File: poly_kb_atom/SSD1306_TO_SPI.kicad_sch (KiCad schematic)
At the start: 12 parts

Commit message: Final version of wave
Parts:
- C1_1, C2_1: value 2.2uF -> (none); footprint Capacitor_SMD:C_0603_1608Metric -> (none)
- C3_1, C5_1, C6_1: value 1uF -> (none); footprint Capacitor_SMD:C_0402_1005Metric -> (none)
- C4_1: value 4.7uF -> (none); footprint Capacitor_SMD:C_0603_1608Metric -> (none)
- C7_1: value DNP -> (none); footprint Capacitor_SMD:C_0603_1608Metric -> (none)
- CONN1: value 0.42" Display Connector -> (none); footprint poly_kb:FPC_16_JUSHUO_AFC05_S16FIA_00 -> (none)
- D1_1: value D_Small -> (none); footprint poly_kb:D_SOD-323Ext -> (none)
- LED1: value WS2812B-Mini -> (none); footprint poly_kb:WS2812B-Mini -> (none)
- R1_1: value 10k -> (none); footprint Resistor_SMD:R_0402_1005Metric -> (none); LCSC (none) -> C25744
- SW_K_1: value CheeryMX KeySwitch -> (none); footprint poly_kb:SW_Cherry_MX_1.00u_PCB_NoSilk -> (none)
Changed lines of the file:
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@@
       (effects (font (size 1.27 1.27)) (justify left))
     )
-    (property "Value" "0.42\" Display Connector" (id 1) (at 76.2 30.48 0)
-      (effects (font (size 1.27 1.27)) (justify left))
-    )
-    (property "Footprint" "poly_kb:FPC_16_JUSHUO_AFC05_S16FIA_00" (id 2) (at 82.55 52.07 0)
+    (property "Value" "" (id 1) (at 76.2 30.48 0)
+      (effects (font (size 1.27 1.27)) (justify left))
+    )
+    (property "Footprint" "" (id 2) (at 82.55 52.07 0)
       (effects (font (size 1.27 1.27)) hide)
     )
@@
     (in_bom yes) (on_board yes)
     (property "Reference" "C6_1" (id 0) (at 63.5 45.72 90))
-    (property "Value" "1uF" (id 1) (at 63.5 48.26 90))
-    (property "Footprint" "Capacitor_SMD:C_0402_1005Metric" (id 2) (at 68.58 46.99 0)
+    (property "Value" "" (id 1) (at 63.5 48.26 90))
+    (property "Footprint" "" (id 2) (at 68.58 46.99 0)
       (effects (font (size 1.27 1.27)) hide)
     )
@@
       (effects (font (size 1.27 1.27)) (justify left))
     )
-    (property "Value" "WS2812B-Mini" (id 1) (at 175.26 54.61 0)
-      (effects (font (size 1.27 1.27)) (justify left))
-    )
-    (property "Footprint" "poly_kb:WS2812B-Mini" (id 2) (at 167.64 55.88 0)
+    (property "Value" "" (id 1) (at 175.26 54.61 0)
+      (effects (font (size 1.27 1.27)) (justify left))
+    )
+    (property "Footprint" "" (id 2) (at 167.64 55.88 0)
       (effects (font (size 1.27 1.27)) (justify left top) hide)
     )
@@
       (effects (font (size 1.27 1.27)) (justify right))
     )
-    (property "Value" "4.7uF" (id 1) (at 57.15 76.2 90)
-      (effects (font (size 1.27 1.27)) (justify right))
-    )
-    (property "Footprint" "Capacitor_SMD:C_0603_1608Metric" (id 2) (at 54.61 69.85 0)
+    (property "Value" "" (id 1) (at 57.15 76.2 90)
+      (effects (font (size 1.27 1.27)) (justify right))
+    )
+    (property "Footprint" "" (id 2) (at 54.61 69.85 0)
       (effects (font (size 1.27 1.27)) hide)
     )
@@
     (in_bom yes) (on_board yes)
     (property "Reference" "C1_1" (id 0) (at 71.12 74.93 0))
-    (property "Value" "2.2uF" (id 1) (at 71.12 77.47 0))
-    (property "Footprint" "Capacitor_SMD:C_0603_1608Metric" (id 2) (at 67.31 74.93 0)
+    (property "Value" "" (id 1) (at 71.12 77.47 0))
+    (property "Footprint" "" (id 2) (at 67.31 74.93 0)
       (effects (font (size 1.27 1.27)) hide)
     )
@@
     (in_bom yes) (on_board yes)
     (property "Reference" "C5_1" (id 0) (at 57.15 36.0934 90))
-    (property "Value" "1uF" (id 1) (at 57.15 38.4048 90))
-    (property "Footprint" "Capacitor_SMD:C_0402_1005Metric" (id 2) (at 57.15 41.91 0)
+    (property "Value" "" (id 1) (at 57.15 38.4048 90))
+    (property "Footprint" "" (id 2) (at 57.15 41.91 0)
       (effects (font (size 1.27 1.27)) hide)
     )
@@
     (in_bom yes) (on_board yes)
     (property "Reference" "C2_1" (id 0) (at 46.99 46.2534 90))
-    (property "Value" "2.2uF" (id 1) (at 46.99 48.5648 90))
-    (property "Footprint" "Capacitor_SMD:C_0603_1608Metric" (id 2) (at 46.99 52.07 0)
+    (property "Value" "" (id 1) (at 46.99 48.5648 90))
+    (property "Footprint" "" (id 2) (at 46.99 52.07 0)
       (effects (font (size 1.27 1.27)) hide)
     )
@@
     (in_bom yes) (on_board yes)
     (property "Reference" "C3_1" (id 0) (at 31.75 42.4434 90))
-    (property "Value" "1uF" (id 1) (at 31.75 44.7548 90))
-    (property "Footprint" "Capacitor_SMD:C_0402_1005Metric" (id 2) (at 31.75 48.26 0)
+    (property "Value" "" (id 1) (at 31.75 44.7548 90))
+    (property "Footprint" "" (id 2) (at 31.75 48.26 0)
       (effects (font (size 1.27 1.27)) hide)
     )
@@
     (in_bom yes) (on_board yes)
     (property "Reference" "SW_K_1" (id 0) (at 129.54 82.931 0))
-    (property "Value" "CheeryMX KeySwitch" (id 1) (at 129.54 85.2424 0))
-    (property "Footprint" "poly_kb:SW_Cherry_MX_1.00u_PCB_NoSilk" (id 2) (at 129.54 85.09 0)
+    (property "Value" "" (id 1) (at 129.54 85.2424 0))
+    (property "Footprint" "" (id 2) (at 129.54 85.09 0)
       (effects (font (size 1.27 1.27)) hide)
     )
@@
     (in_bom yes) (on_board yes)
     (property "Reference" "D1_1" (id 0) (at 139.7 95.4278 0))
-    (property "Value" "D_Small" (id 1) (at 139.7 93.1164 0))
-    (property "Footprint" "poly_kb:D_SOD-323Ext" (id 2) (at 139.7 90.17 90)
+    (property "Value" "" (id 1) (at 139.7 93.1164 0))
+    (property "Footprint" "" (id 2) (at 139.7 90.17 90)
       (effects (font (size 1.27 1.27)) hide)
     )
@@
       (effects (font (size 1.27 1.27)) (justify right))
     )
-    (property "Value" "DNP" (id 1) (at 142.24 45.72 0)
-      (effects (font (size 1.27 1.27)) (justify right))
-    )
-    (property "Footprint" "Capacitor_SMD:C_0603_1608Metric" (id 2) (at 142.24 48.26 0)
+    (property "Value" "" (id 1) (at 142.24 45.72 0)
+      (effects (font (size 1.27 1.27)) (justify right))
+    )
+    (property "Footprint" "" (id 2) (at 142.24 48.26 0)
       (effects (font (size 1.27 1.27)) hide)
     )
@@
       (effects (font (size 1.27 1.27)) (justify left))
     )
-    (property "Value" "10k" (id 1) (at 34.5186 58.293 0)
-      (effects (font (size 1.27 1.27)) (justify left))
-    )
-    (property "Footprint" "Resistor_SMD:R_0402_1005Metric" (id 2) (at 33.02 57.15 0)
+    (property "Value" "" (id 1) (at 34.5186 58.293 0)
+      (effects (font (size 1.27 1.27)) (justify left))
+    )
+    (property "Footprint" "" (id 2) (at 33.02 57.15 0)
       (effects (font (size 1.27 1.27)) hide)
     )
@@
       (effects (font (size 1.27 1.27)) hide)
     )
+    (property "LCSC" "C25744" (id 4) (at 33.02 57.15 0)
+      (effects (font (size 1.27 1.27)) hide)
+    )

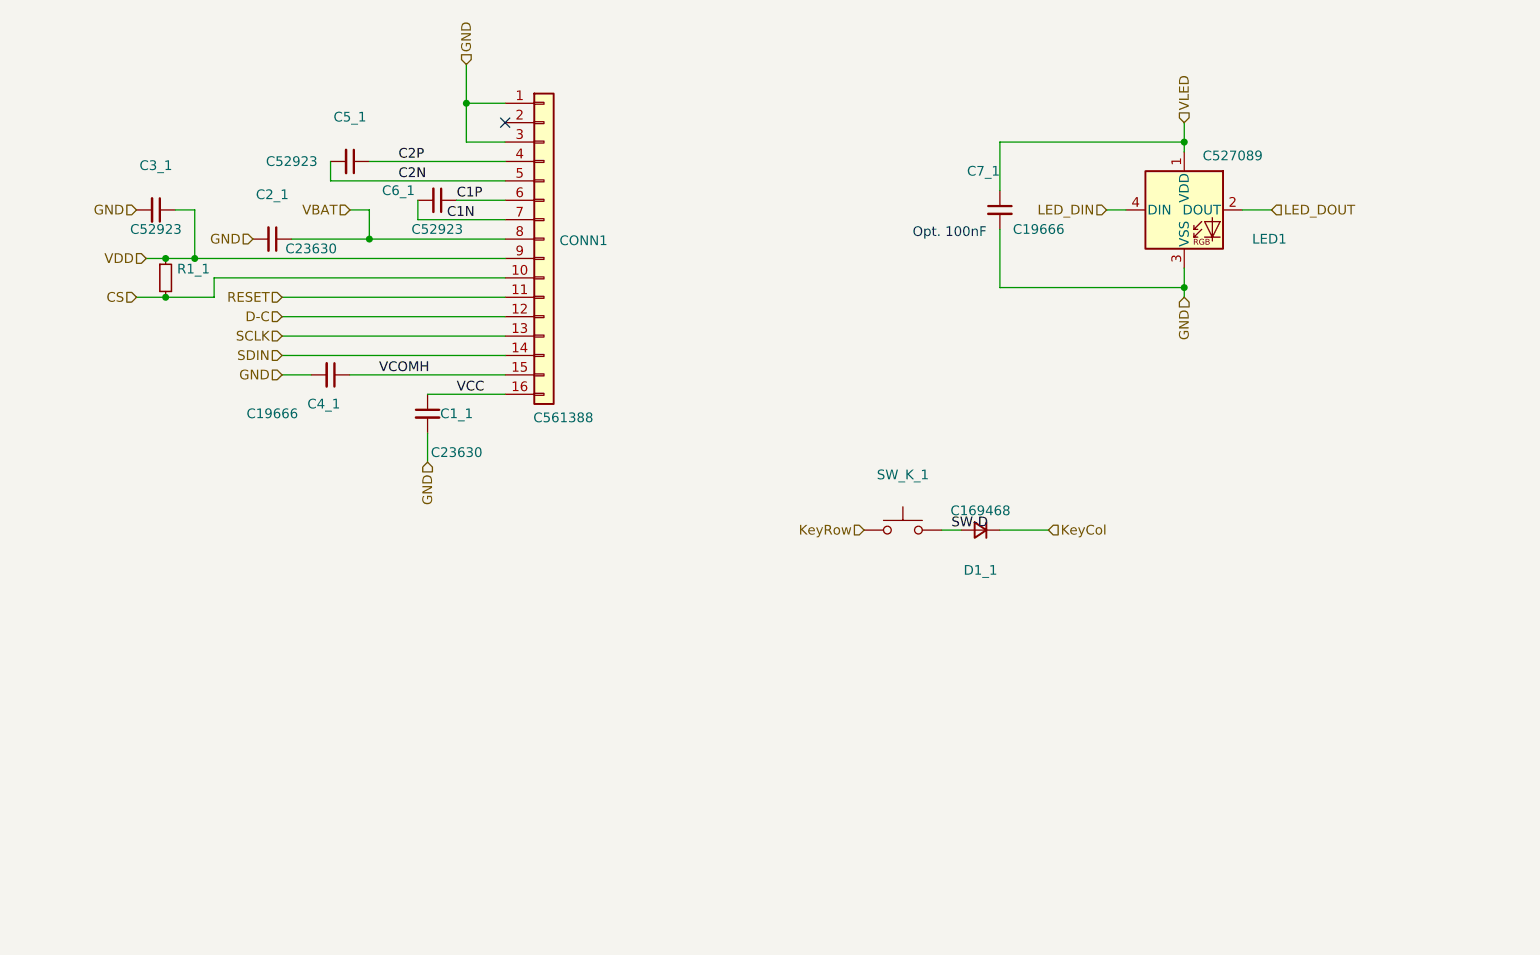
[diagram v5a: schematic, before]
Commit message: Added power leds
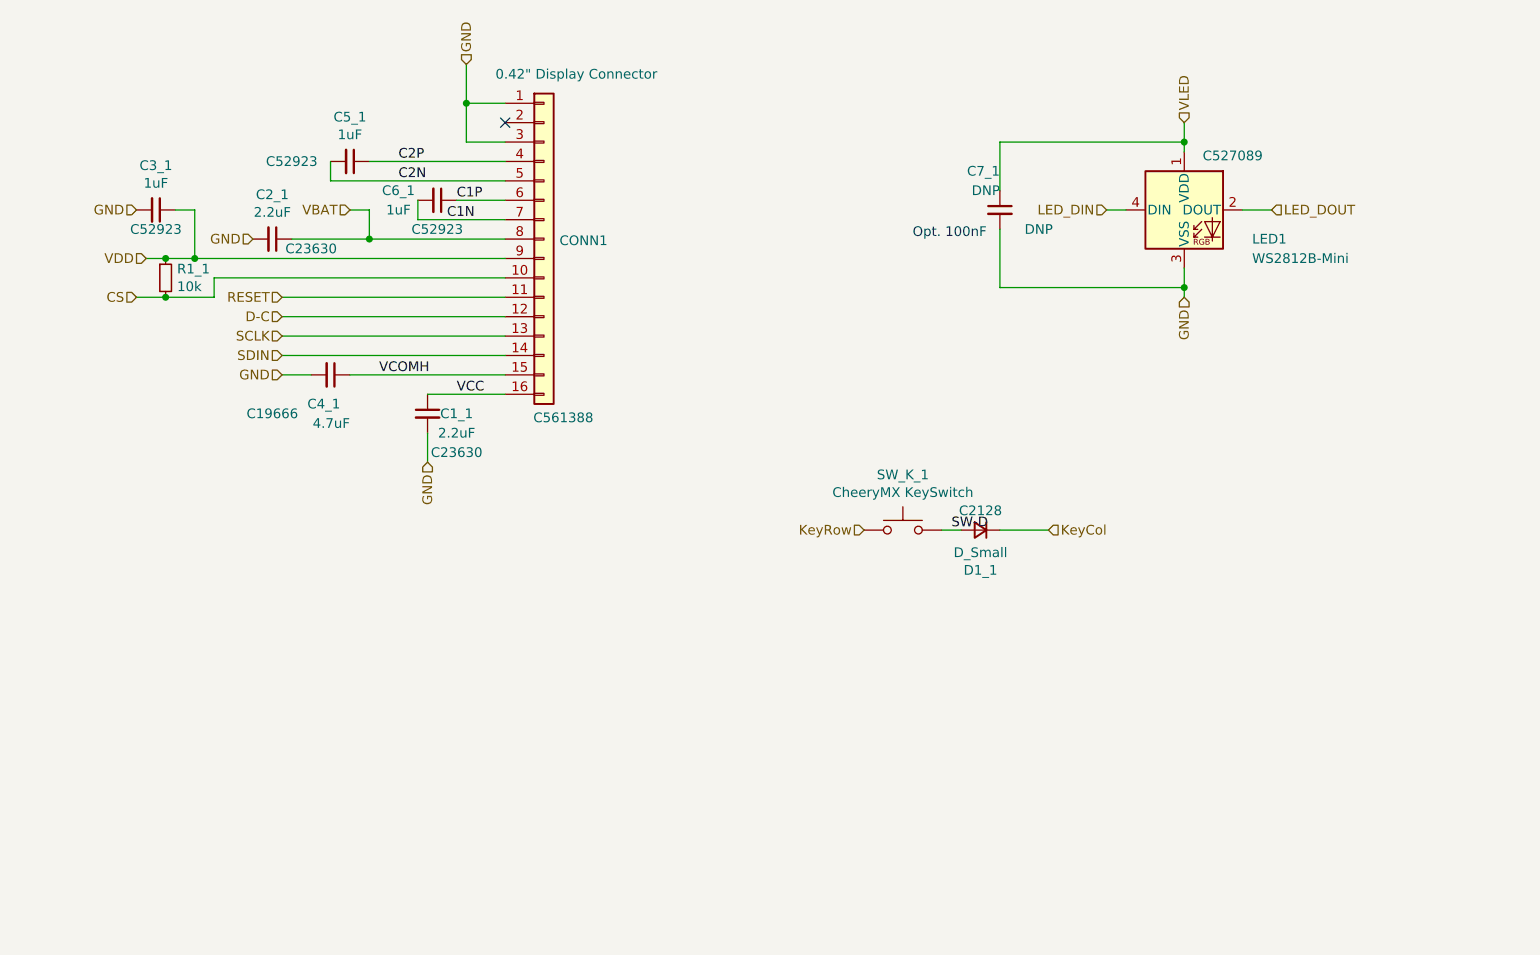
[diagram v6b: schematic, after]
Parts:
- C1_1, C2_1: value (none) -> 2.2uF; JLC (none) -> 0603; LCSC C23630 -> C23630
- C3_1, C5_1, C6_1: value (none) -> 1uF; JLC (none) -> 0402; LCSC C52923 -> C52923
- C4_1: value (none) -> 4.7uF; JLC (none) -> 0603
- C7_1: value (none) -> DNP; JLC (none) -> DNP; LCSC C19666 -> DNP
- CONN1: value (none) -> 0.42" Display Connector; JLC (none) -> AtomConnect2
- D1_1: value (none) -> D_Small; JLC (none) -> D_SOD-323Ext; LCSC C169468 -> C2128
- LED1: value (none) -> WS2812B-Mini; JLC (none) -> WS2812B-Mini
- R1_1: value (none) -> 10k; JLC (none) -> 0402
- SW_K_1: value (none) -> CheeryMX KeySwitch
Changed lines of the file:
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@@
       (effects (font (size 1.27 1.27)) (justify left))
     )
-    (property "Value" "" (id 1) (at 76.2 30.48 0)
+    (property "Value" "0.42\" Display Connector" (id 1) (at 76.2 30.48 0)
       (effects (font (size 1.27 1.27)) (justify left))
     )
@@
     (property "LCSC" "C561388" (id 4) (at 85.09 76.2 0)
       (effects (font (size 1.27 1.27)) (justify bottom))
+    )
+    (property "JLC" "AtomConnect2" (id 5) (at 82.55 52.07 0)
+      (effects (font (size 1.27 1.27)) hide)
     )
     (pin "1")
@@
     (in_bom yes) (on_board yes)
     (property "Reference" "C6_1" (id 0) (at 63.5 45.72 90))
-    (property "Value" "" (id 1) (at 63.5 48.26 90))
+    (property "Value" "1uF" (id 1) (at 63.5 48.26 90))
     (property "Footprint" "" (id 2) (at 68.58 46.99 0)
       (effects (font (size 1.27 1.27)) hide)
@@
       (effects (font (size 1.27 1.27)) hide)
     )
-    (property "LCSC" " C52923" (id 4) (at 68.58 50.8 90))
+    (property "LCSC" "C52923" (id 4) (at 68.58 50.8 90))
+    (property "JLC" "0402" (id 5) (at 68.58 46.99 0)
+      (effects (font (size 1.27 1.27)) hide)
+    )
     (pin "1")
     (pin "2")
@@
       (effects (font (size 1.27 1.27)) (justify left))
     )
-    (property "Value" "" (id 1) (at 175.26 54.61 0)
+    (property "Value" "WS2812B-Mini" (id 1) (at 175.26 54.61 0)
       (effects (font (size 1.27 1.27)) (justify left))
     )
@@
       (effects (font (size 1.27 1.27)) (justify bottom))
     )
+    (property "JLC" "WS2812B-Mini" (id 5) (at 166.37 48.26 0)
+      (effects (font (size 1.27 1.27)) hide)
+    )
     (pin "1")
     (pin "2")
@@
       (effects (font (size 1.27 1.27)) (justify right))
     )
-    (property "Value" "" (id 1) (at 57.15 76.2 90)
+    (property "Value" "4.7uF" (id 1) (at 57.15 76.2 90)
       (effects (font (size 1.27 1.27)) (justify right))
     )
@@
     )
     (property "LCSC" "C19666" (id 4) (at 46.99 74.93 90))
+    (property "JLC" "0603" (id 5) (at 54.61 69.85 0)
+      (effects (font (size 1.27 1.27)) hide)
+    )
     (pin "1")
     (pin "2")
@@
     (in_bom yes) (on_board yes)
     (property "Reference" "C1_1" (id 0) (at 71.12 74.93 0))
-    (property "Value" "" (id 1) (at 71.12 77.47 0))
+    (property "Value" "2.2uF" (id 1) (at 71.12 77.47 0))
     (property "Footprint" "" (id 2) (at 67.31 74.93 0)
       (effects (font (size 1.27 1.27)) hide)
@@
       (effects (font (size 1.27 1.27)) hide)
     )
-    (property "LCSC" " C23630" (id 4) (at 71.12 80.01 0))
+    (property "LCSC" "C23630" (id 4) (at 71.12 80.01 0))
+    (property "JLC" "0603" (id 5) (at 67.31 74.93 0)
+      (effects (font (size 1.27 1.27)) hide)
+    )
     (pin "1")
     (pin "2")
@@
     (in_bom yes) (on_board yes)
     (property "Reference" "C5_1" (id 0) (at 57.15 36.0934 90))
-    (property "Value" "" (id 1) (at 57.15 38.4048 90))
+    (property "Value" "1uF" (id 1) (at 57.15 38.4048 90))
     (property "Footprint" "" (id 2) (at 57.15 41.91 0)
       (effects (font (size 1.27 1.27)) hide)
@@
       (effects (font (size 1.27 1.27)) hide)
     )
-    (property "LCSC" " C52923" (id 4) (at 49.53 41.91 90))
+    (property "LCSC" "C52923" (id 4) (at 49.53 41.91 90))
+    (property "JLC" "0402" (id 5) (at 57.15 41.91 0)
+      (effects (font (size 1.27 1.27)) hide)
+    )
     (pin "1")
     (pin "2")
@@
     (in_bom yes) (on_board yes)
     (property "Reference" "C2_1" (id 0) (at 46.99 46.2534 90))
-    (property "Value" "" (id 1) (at 46.99 48.5648 90))
+    (property "Value" "2.2uF" (id 1) (at 46.99 48.5648 90))
     (property "Footprint" "" (id 2) (at 46.99 52.07 0)
       (effects (font (size 1.27 1.27)) hide)
@@
       (effects (font (size 1.27 1.27)) hide)
     )
-    (property "LCSC" " C23630" (id 4) (at 52.07 53.34 90))
+    (property "LCSC" "C23630" (id 4) (at 52.07 53.34 90))
+    (property "JLC" "0603" (id 5) (at 46.99 52.07 0)
+      (effects (font (size 1.27 1.27)) hide)
+    )
     (pin "1")
     (pin "2")
@@
     (in_bom yes) (on_board yes)
     (property "Reference" "C3_1" (id 0) (at 31.75 42.4434 90))
-    (property "Value" "" (id 1) (at 31.75 44.7548 90))
+    (property "Value" "1uF" (id 1) (at 31.75 44.7548 90))
     (property "Footprint" "" (id 2) (at 31.75 48.26 0)
       (effects (font (size 1.27 1.27)) hide)
@@
       (effects (font (size 1.27 1.27)) hide)
     )
-    (property "LCSC" " C52923" (id 4) (at 31.75 50.8 90))
+    (property "LCSC" "C52923" (id 4) (at 31.75 50.8 90))
+    (property "JLC" "0402" (id 5) (at 31.75 48.26 0)
+      (effects (font (size 1.27 1.27)) hide)
+    )
     (pin "1")
     (pin "2")
@@
     (in_bom yes) (on_board yes)
     (property "Reference" "SW_K_1" (id 0) (at 129.54 82.931 0))
-    (property "Value" "" (id 1) (at 129.54 85.2424 0))
+    (property "Value" "CheeryMX KeySwitch" (id 1) (at 129.54 85.2424 0))
     (property "Footprint" "" (id 2) (at 129.54 85.09 0)
       (effects (font (size 1.27 1.27)) hide)
@@
     (in_bom yes) (on_board yes)
     (property "Reference" "D1_1" (id 0) (at 139.7 95.4278 0))
-    (property "Value" "" (id 1) (at 139.7 93.1164 0))
+    (property "Value" "D_Small" (id 1) (at 139.7 93.1164 0))
     (property "Footprint" "" (id 2) (at 139.7 90.17 90)
       (effects (font (size 1.27 1.27)) hide)
@@
       (effects (font (size 1.27 1.27)) hide)
     )
-    (property "LCSC" "C169468" (id 4) (at 139.7 87.63 0))
+    (property "LCSC" "C2128" (id 4) (at 139.7 87.63 0))
+    (property "JLC" "D_SOD-323Ext" (id 5) (at 139.7 90.17 0)
+      (effects (font (size 1.27 1.27)) hide)
+    )
     (pin "1")
     (pin "2")
@@
       (effects (font (size 1.27 1.27)) (justify right))
     )
-    (property "Value" "" (id 1) (at 142.24 45.72 0)
+    (property "Value" "DNP" (id 1) (at 142.24 45.72 0)
       (effects (font (size 1.27 1.27)) (justify right))
     )
@@
       (effects (font (size 1.27 1.27)) hide)
     )
-    (property "Datasheet" "~" (id 3) (at 142.24 48.26 0)
-      (effects (font (size 1.27 1.27)) hide)
-    )
-    (property "LCSC" "C19666" (id 4) (at 147.32 50.8 0))
+    (property "Datasheet" "C19666" (id 3) (at 142.24 48.26 0)
+      (effects (font (size 1.27 1.27)) hide)
+    )
+    (property "LCSC" "DNP" (id 4) (at 147.32 50.8 0))
+    (property "JLC" "DNP" (id 5) (at 142.24 48.26 0)
+      (effects (font (size 1.27 1.27)) hide)
+    )
     (pin "1")
     (pin "2")
@@
       (effects (font (size 1.27 1.27)) (justify left))
     )
-    (property "Value" "" (id 1) (at 34.5186 58.293 0)
+    (property "Value" "10k" (id 1) (at 34.5186 58.293 0)
       (effects (font (size 1.27 1.27)) (justify left))
     )
@@
       (effects (font (size 1.27 1.27)) hide)
     )
+    (property "JLC" "0402" (id 5) (at 33.02 57.15 0)
+      (effects (font (size 1.27 1.27)) hide)
+    )
